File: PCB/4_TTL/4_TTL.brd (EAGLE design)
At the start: 67.4 x 44.5 mm, 3 parts, among them J1 MA03-1W, X10 ALLSERIALD, X5 AKL18X-10W

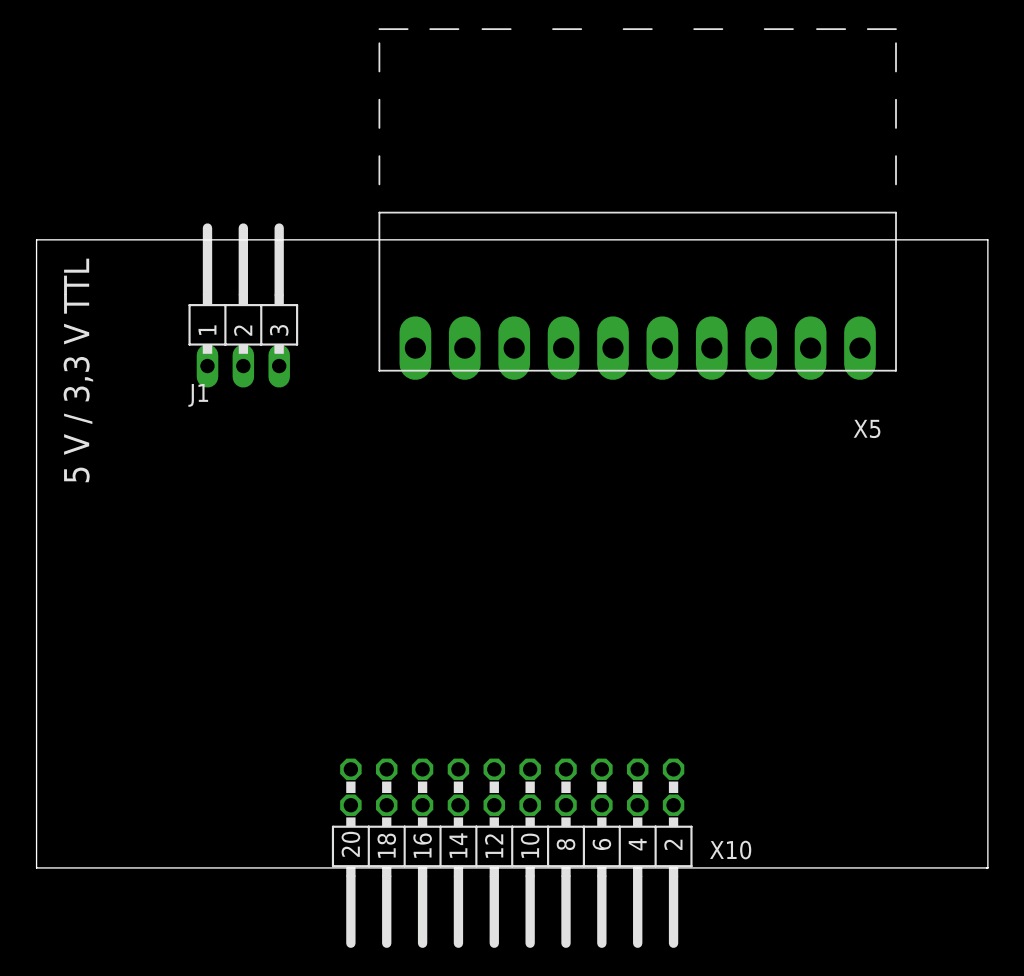
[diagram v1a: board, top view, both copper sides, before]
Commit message: Improve lib
Route RS232 board
Route TTL board
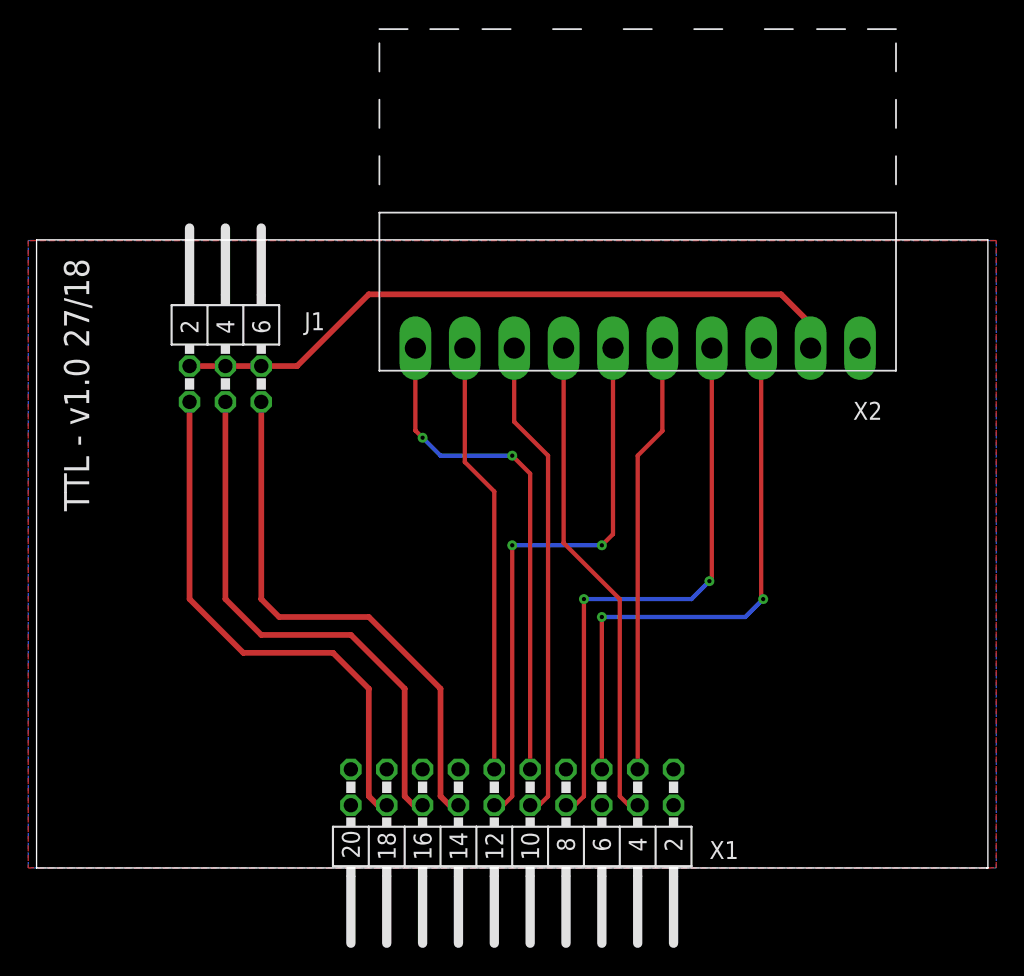
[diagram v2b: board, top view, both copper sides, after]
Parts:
- J1: value MA03-1W -> MA03-2W; device con-lstb:MA03-1W -> con-lstb:MA03-2W
- moved J1 1.80 mm to (-20.3, 34.3)
- renumbered X10 to X1, X5 to X2
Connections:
- removed net N$47: J1.1, X1.16
- removed net N$71: J1.3, X1.18
- removed net N$90: J1.2, X1.7, X2.P$2
- new net N$1: J1.2, J1.4, J1.6, X2.P$2
- new net N$2: J1.5, X1.14
- new net N$3: J1.3, X1.16
- new net N$4: J1.1, X1.18
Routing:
- net N$1: track 0.00 -> 48.7 mm
- net RXD4: track 0.00 -> 41.5 mm, vias 0 -> 2
- net TXD4: track 0.00 -> 40.6 mm, vias 0 -> 2
- net CTS4: track 0.00 -> 40.0 mm, vias 0 -> 2
- net N$4: track 0.00 -> 38.5 mm
- net N$3: track 0.00 -> 38.5 mm
- net N$2: track 0.00 -> 38.5 mm
- net RI4: track 0.00 -> 36.2 mm, vias 0 -> 2
- net DTR4: track 0.00 -> 34.9 mm
- net DSR4: track 0.00 -> 34.3 mm
- net DCD4: track 0.00 -> 30.7 mm
- net RTS4: track 0.00 -> 30.6 mm
- added copper zone on layer 1, net GND
- added copper zone on layer 16, net GND
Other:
- board text added: "TTL - v1.0 27/18"
- board text removed: "5 V / 3,3 V TTL"
